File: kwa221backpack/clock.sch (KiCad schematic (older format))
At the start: 5 parts, among them P1 CONN_01X10, P2 CONN_01X10, U1 TLC5940NT

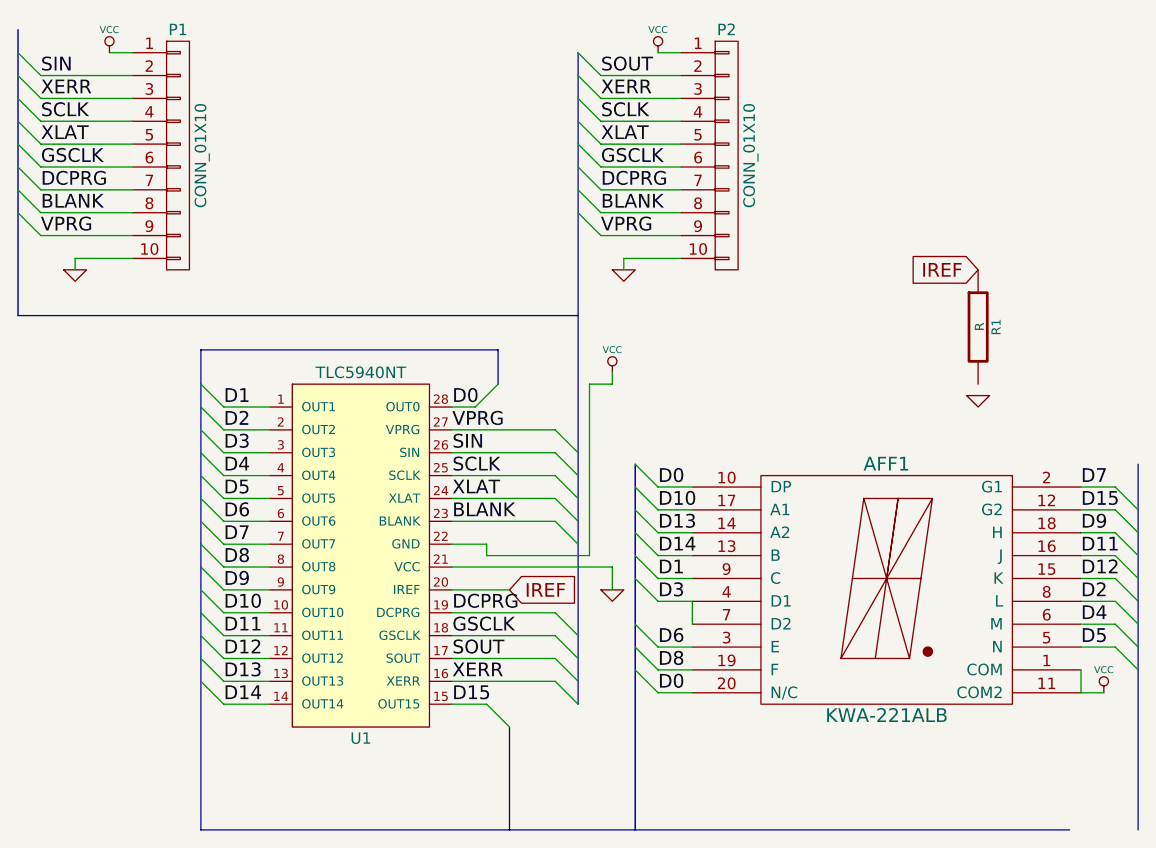
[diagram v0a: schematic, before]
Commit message: Re-order pins on header to simplify chip routing
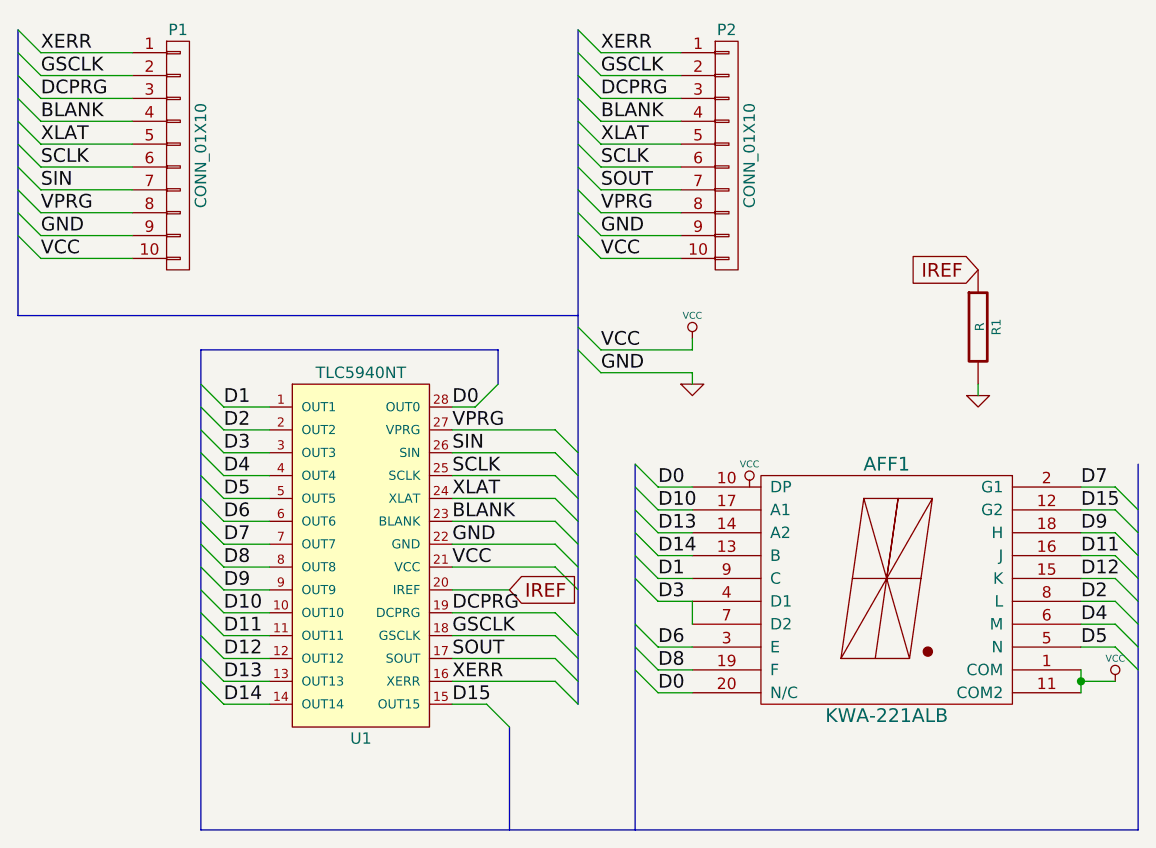
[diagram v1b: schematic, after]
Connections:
- net BLANK: now also P1.4 (P4), P2.4 (P4); no longer P1.8 (P8), P2.8 (P8)
- net DCPRG: now also P1.3 (P3), P2.3 (P3); no longer P1.7 (P7), P2.7 (P7)
- net GND: now also P1.9 (P9), P2.9 (P9), R1.2, U1.22 (GND); no longer P1.10 (P10), P2.10 (P10), U1.21 (VCC)
- net GSCLK: now also P1.2 (P2), P2.2 (P2); no longer P1.6 (P6), P2.6 (P6)
- net SCLK: now also P1.6 (P6), P2.6 (P6); no longer P1.4 (P4), P2.4 (P4)
- net SIN: now also P1.7 (P7); no longer P1.2 (P2)
- net SOUT: now also P2.7 (P7); no longer P2.2 (P2)
- net VCC: now also P1.10 (P10), P2.10 (P10), U1.21 (VCC); no longer P1.1 (P1), P2.1 (P1), U1.22 (GND)
- net VPRG: now also P1.8 (P8), P2.8 (P8); no longer P1.9 (P9), P2.9 (P9)
- net XERR: now also P1.1 (P1), P2.1 (P1); no longer P1.3 (P3), P2.3 (P3)
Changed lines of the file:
@@
 	3300 3700 3400 3800
-$Comp
-L GND #PWR01
-U 1 1 540E56BB
-P 3250 2050
-F 0 "#PWR01" H 3250 2050 30  0001 C CNN
-F 1 "GND" H 3250 1980 30  0001 C CNN
-F 2 "" H 3250 2050 60  0000 C CNN
-F 3 "" H 3250 2050 60  0000 C CNN
-	1    3250 2050
-	1    0    0    -1
-$EndComp
-$Comp
-L VCC #PWR02
-U 1 1 540E573D
-P 3400 1100
-F 0 "#PWR02" H 3400 1200 30  0001 C CNN
-F 1 "VCC" H 3400 1200 30  0000 C CNN
-F 2 "" H 3400 1100 60  0000 C CNN
-F 3 "" H 3400 1100 60  0000 C CNN
-	1    3400 1100
-	1    0    0    -1
-$EndComp
 $Comp
 L CONN_01X10 P2
@@
 $EndComp
 $Comp
-L GND #PWR03
-U 1 1 540E5D45
-P 850 2050
-F 0 "#PWR03" H 850 2050 30  0001 C CNN
-F 1 "GND" H 850 1980 30  0001 C CNN
-F 2 "" H 850 2050 60  0000 C CNN
-F 3 "" H 850 2050 60  0000 C CNN
-	1    850  2050
-	1    0    0    -1
-$EndComp
-$Comp
-L VCC #PWR04
-U 1 1 540E5D4B
-P 1000 1100
-F 0 "#PWR04" H 1000 1200 30  0001 C CNN
-F 1 "VCC" H 1000 1200 30  0000 C CNN
-F 2 "" H 1000 1100 60  0000 C CNN
-F 3 "" H 1000 1100 60  0000 C CNN
-	1    1000 1100
-	1    0    0    -1
-$EndComp
-$Comp
 L CONN_01X10 P1
 U 1 1 540E5D54
@@
 SIN
 Text Label 700  1200 0    60   ~ 0
-SIN
+GSCLK
 Text Label 3150 1200 0    60   ~ 0
-SOUT
+GSCLK
 Text Label 2500 3050 0    60   ~ 0
 XLAT
@@
 SCLK
 Text Label 700  1300 0    60   ~ 0
-XERR
+DCPRG
 Text Label 700  1400 0    60   ~ 0
-SCLK
+BLANK
 Text Label 700  1500 0    60   ~ 0
 XLAT
 Text Label 700  1600 0    60   ~ 0
-GSCLK
+SCLK
 Text Label 700  1700 0    60   ~ 0
+SIN
+Text Label 700  1800 0    60   ~ 0
+VPRG
+Text Label 700  1900 0    60   ~ 0
+GND
+Text Label 3150 1300 0    60   ~ 0
 DCPRG
-Text Label 700  1800 0    60   ~ 0
+Text Label 3150 1400 0    60   ~ 0
 BLANK
-Text Label 700  1900 0    60   ~ 0
-VPRG
-Text Label 3150 1300 0    60   ~ 0
-XERR
-Text Label 3150 1400 0    60   ~ 0
-SCLK
 Text Label 3150 1500 0    60   ~ 0
 XLAT
 Text Label 3150 1600 0    60   ~ 0
-GSCLK
+SCLK
 Text Label 3150 1700 0    60   ~ 0
-DCPRG
+SOUT
 Text Label 3150 1800 0    60   ~ 0
-BLANK
+VPRG
 Text Label 3150 1900 0    60   ~ 0
-VPRG
+GND
 Text Label 1500 3250 0    60   ~ 0
 D7
@@
 	1400 2400 1400 4500
 Wire Bus Line
-	5500 2900 5500 4500
+	5500 4500 5500 2900
 Wire Bus Line
 	3300 2900 3300 4500
 Wire Bus Line
-	1400 4500 5200 4500
+	1400 4500 5500 4500
 Wire Wire Line
 	1700 3250 1500 3250
@@
 	2500 3450 2750 3450
 Wire Wire Line
-	2500 3350 3200 3350
-Wire Wire Line
-	2500 3250 2650 3250
-Wire Wire Line
 	3400 3000 3550 3000
 Wire Wire Line
@@
 Wire Wire Line
 	3400 3800 3550 3800
-Wire Wire Line
-	3250 2000 3500 2000
-Wire Wire Line
-	3250 2000 3250 2050
-Wire Wire Line
-	3500 1100 3400 1100
-Wire Wire Line
-	850  2000 1100 2000
-Wire Wire Line
-	850  2000 850  2050
-Wire Wire Line
-	1100 1100 1000 1100
 Wire Bus Line
 	600  1000 600  2250
@@
 	5250 3800 5250 3900
 Wire Wire Line
-	5250 3900 5350 3900
-$Comp
-L VCC #PWR05
-U 1 1 540E6D9B
-P 5350 3900
-F 0 "#PWR05" H 5350 4000 30  0001 C CNN
-F 1 "VCC" H 5350 4000 30  0000 C CNN
-F 2 "" H 5350 3900 60  0000 C CNN
-F 3 "" H 5350 3900 60  0000 C CNN
-	1    5350 3900
-	1    0    0    -1
-$EndComp
-$Comp
-L VCC #PWR06
-U 1 1 540E6E29
-P 3200 2500
-F 0 "#PWR06" H 3200 2600 30  0001 C CNN
-F 1 "VCC" H 3200 2600 30  0000 C CNN
-F 2 "" H 3200 2500 60  0000 C CNN
-F 3 "" H 3200 2500 60  0000 C CNN
-	1    3200 2500
-	1    0    0    -1
-$EndComp
-Wire Wire Line
-	3100 2550 3200 2550
-Wire Wire Line
-	3200 2550 3200 2500
+	3550 2400 3150 2400
 $Comp
 L TLC5940NT U1
@@
 $EndComp
 Wire Bus Line
-	3050 1100 3050 3950
+	3050 1000 3050 3950
 Entry Wire Line
 	1400 2550 1500 2650
@@
 Text Label 2500 2750 0    60   ~ 0
 VPRG
-Wire Wire Line
-	3100 3300 3100 2550
-Wire Wire Line
-	2650 3250 2650 3300
-Wire Wire Line
-	3200 3350 3200 3450
-$Comp
-L GND #PWR07
-U 1 1 540E8157
-P 3200 3450
-F 0 "#PWR07" H 3200 3450 30  0001 C CNN
-F 1 "GND" H 3200 3380 30  0001 C CNN
-F 2 "" H 3200 3450 60  0000 C CNN
-F 3 "" H 3200 3450 60  0000 C CNN
-	1    3200 3450
-	1    0    0    -1
-$EndComp
-Wire Wire Line
-	2650 3300 3100 3300
 Entry Wire Line
 	3300 3800 3400 3900
@@
 IREF
 $Comp
-L GND #PWR08
+L GND #PWR01
 U 1 1 540F12D2
 P 4800 2600
-F 0 "#PWR08" H 4800 2600 30  0001 C CNN
+F 0 "#PWR01" H 4800 2600 30  0001 C CNN
 F 1 "GND" H 4800 2530 30  0001 C CNN
 F 2 "" H 4800 2600 60  0000 C CNN
@@
 	1    0    0    -1
 $EndComp
+Wire Wire Line
+	4800 2550 4800 2600
+Entry Wire Line
+	600  1000 700  1100
+Entry Wire Line
+	600  1900 700  2000
+Wire Wire Line
+	1100 1100 700  1100
+Wire Wire Line
+	1100 2000 700  2000
+Entry Wire Line
+	3050 1000 3150 1100
+Entry Wire Line
+	3050 1900 3150 2000
+Wire Wire Line
+	3150 2000 3500 2000
+Wire Wire Line
+	3150 1100 3500 1100
+Entry Wire Line
+	3050 2300 3150 2400
+Entry Wire Line
+	3050 2400 3150 2500
+$Comp
+L GND #PWR02
+U 1 1 540F2AA5
+P 3550 2550
+F 0 "#PWR02" H 3550 2550 30  0001 C CNN
+F 1 "GND" H 3550 2480 30  0001 C CNN
+F 2 "" H 3550 2550 60  0000 C CNN
+F 3 "" H 3550 2550 60  0000 C CNN
+	1    3550 2550
+	1    0    0    -1
+$EndComp
+Text Label 3150 2400 0    60   ~ 0
+VCC
+Text Label 3150 2500 0    60   ~ 0
+GND
+Wire Wire Line
+	3150 2500 3550 2500
+Wire Wire Line
+	3550 2500 3550 2550
+$Comp
+L VCC #PWR03
+U 1 1 540F2B77
+P 3550 2350
+F 0 "#PWR03" H 3550 2450 30  0001 C CNN
+F 1 "VCC" H 3550 2450 30  0000 C CNN
+F 2 "" H 3550 2350 60  0000 C CNN
+F 3 "" H 3550 2350 60  0000 C CNN
+	1    3550 2350
+	1    0    0    -1
+$EndComp
+Wire Wire Line
+	3550 2400 3550 2350
+Entry Wire Line
+	2950 3250 3050 3350
+Entry Wire Line
+	2950 3350 3050 3450
+Wire Wire Line
+	2500 3250 2950 3250
+Wire Wire Line
+	2950 3350 2500 3350
+Text Label 2500 3250 0    60   ~ 0
+GND
+Text Label 2500 3350 0    60   ~ 0
+VCC
+$Comp
+L VCC #PWR04
+U 1 1 540F2CCB
+P 3800 3000
+F 0 "#PWR04" H 3800 3100 30  0001 C CNN
+F 1 "VCC" H 3800 3100 30  0000 C CNN
+F 2 "" H 3800 3000 60  0000 C CNN
+F 3 "" H 3800 3000 60  0000 C CNN
+	1    3800 3000
+	1    0    0    -1
+$EndComp
+$Comp
+L VCC #PWR05
+U 1 1 540F2CDA
+P 5400 3850
+F 0 "#PWR05" H 5400 3950 30  0001 C CNN
+F 1 "VCC" H 5400 3950 30  0000 C CNN
+F 2 "" H 5400 3850 60  0000 C CNN
+F 3 "" H 5400 3850 60  0000 C CNN
+	1    5400 3850
+	1    0    0    -1
+$EndComp
+Wire Wire Line
+	5400 3850 5250 3850
+Connection ~ 5250 3850
+Text Label 700  1100 0    60   ~ 0
+XERR
+Text Label 3150 1100 0    60   ~ 0
+XERR
+Text Label 3150 2000 0    60   ~ 0
+VCC
+Text Label 700  2000 0    60   ~ 0
+VCC
 $EndSCHEMATC

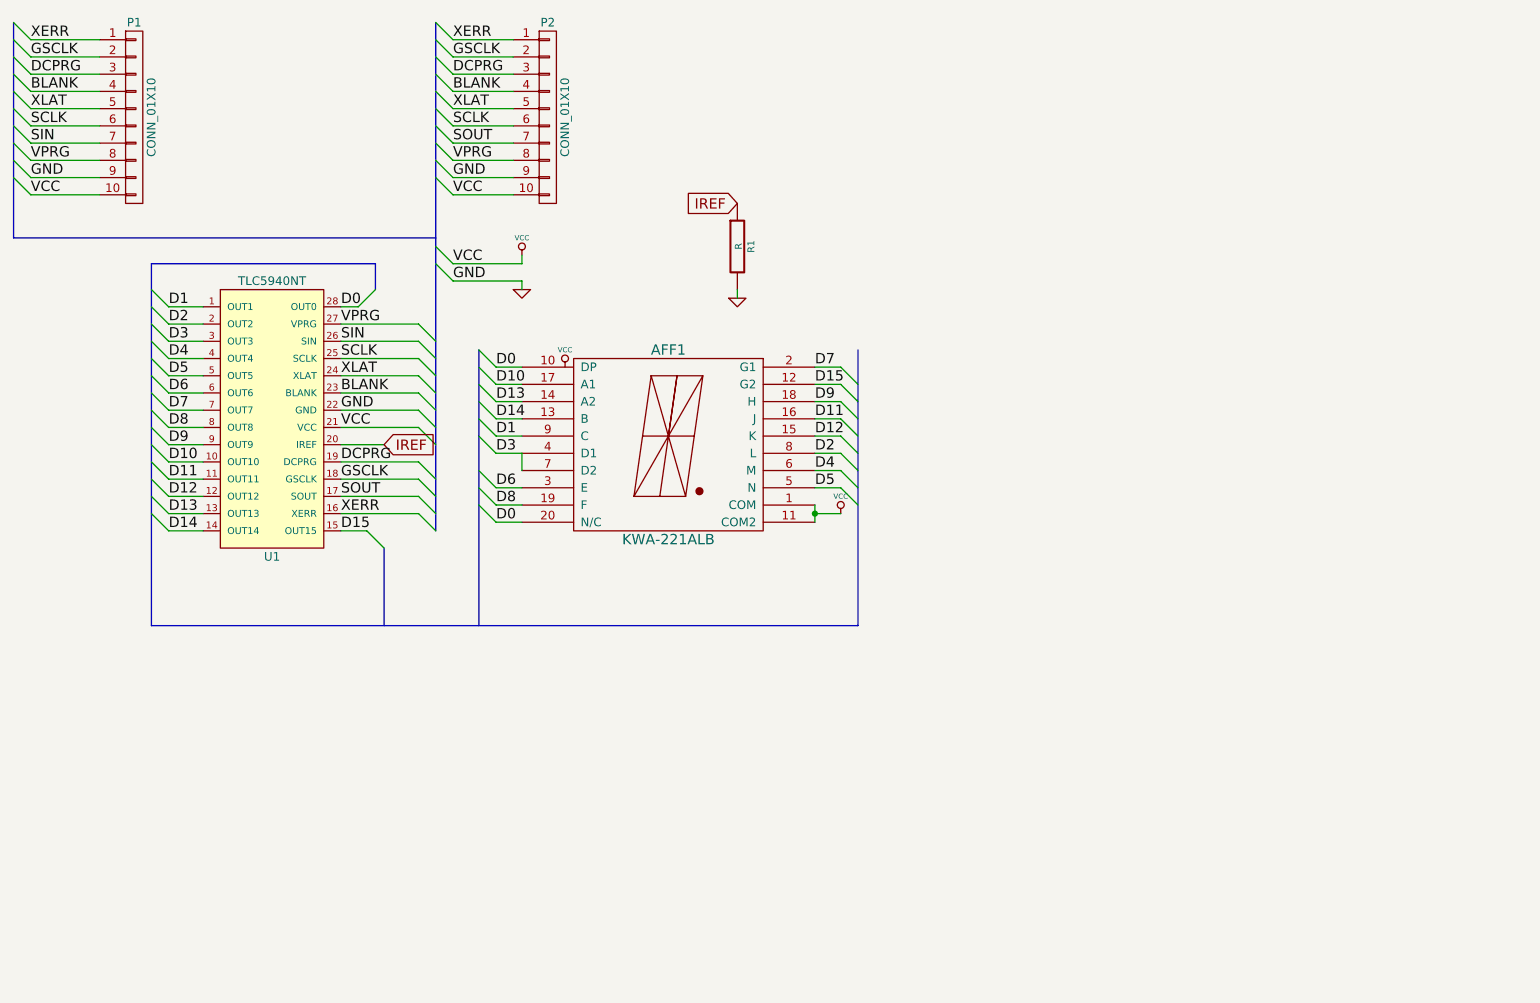
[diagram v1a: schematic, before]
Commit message: Update schematic for v2: mounting holes and test point to measure iref resistor
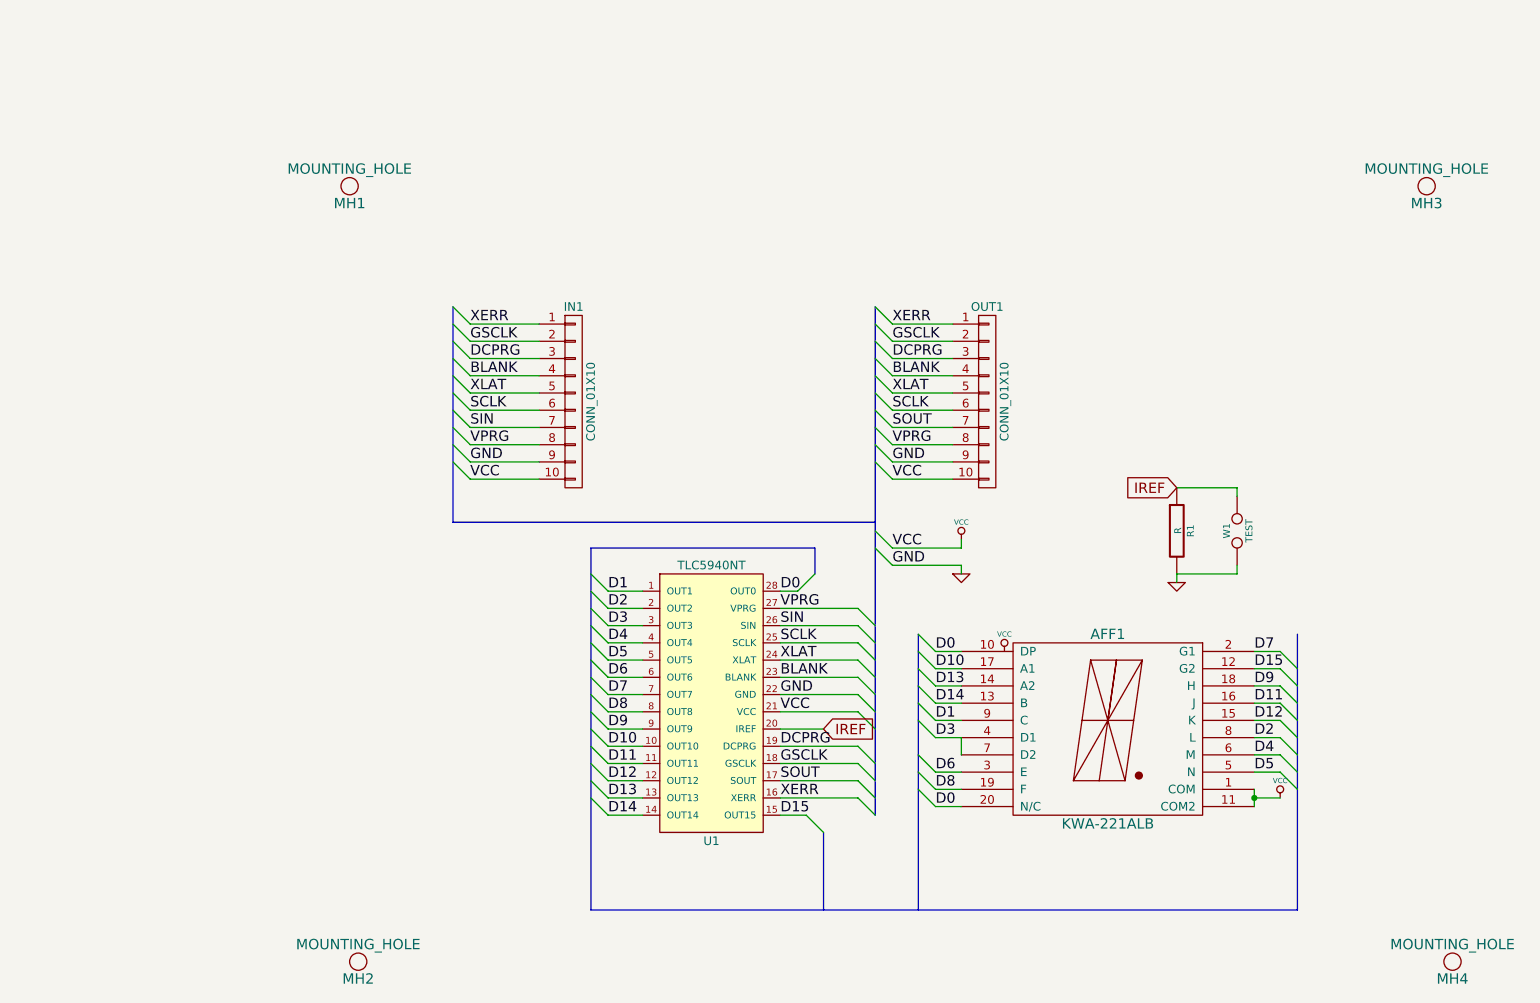
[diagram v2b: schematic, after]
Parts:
- added MH1, MH2, MH3, MH4: MOUNTING_HOLE, symbol MOUNTING_HOLE
- added W1: TEST, symbol TEST
- renumbered P1 to IN1, P2 to OUT1
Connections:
- net GND: now also W1.1
- net IREF: now also W1.2
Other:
- moved on the sheet: AFF1, IN1, OUT1, R1, U1
